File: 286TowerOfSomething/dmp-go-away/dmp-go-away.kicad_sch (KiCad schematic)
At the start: 2 parts, among them J1 Bus_ISA_16bit, U1 M6117C

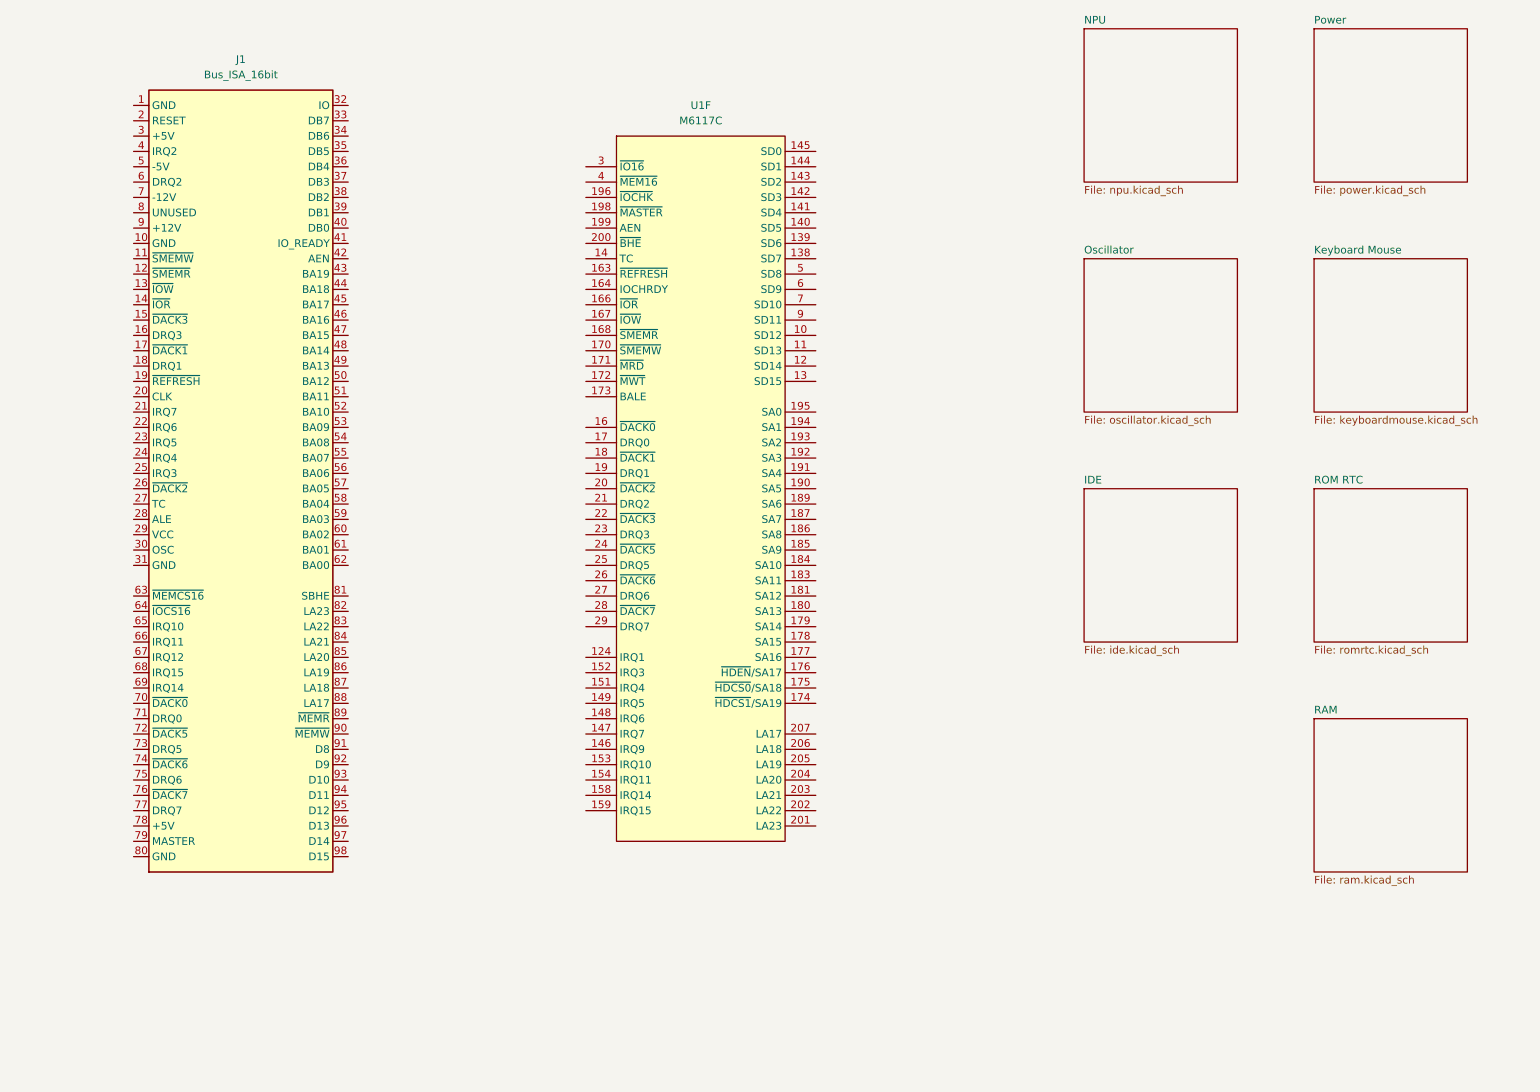
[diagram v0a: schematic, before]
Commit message: Adding work done on 386 card, coming along nicely
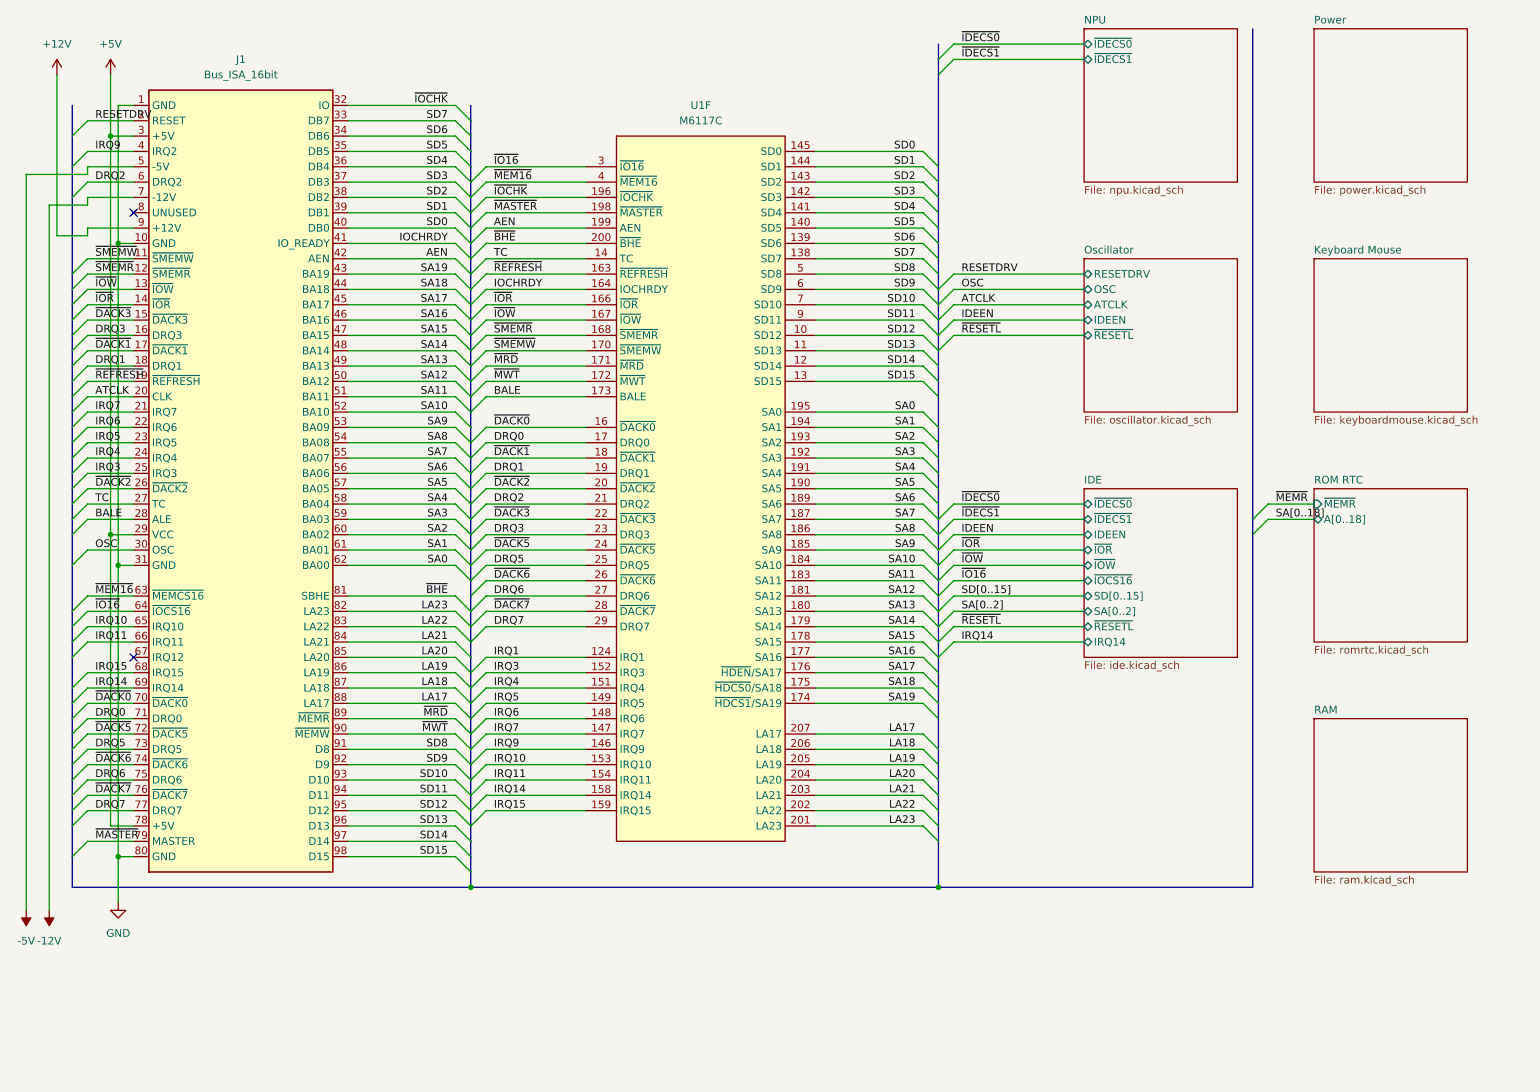
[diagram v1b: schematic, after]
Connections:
- net GND: now reaches J1.1 (GND)
- net GND: now also J1.10 (GND), J1.31 (GND), J1.80 (GND)
- net ~{SMEMW}: now reaches J1.11 (~{SMEMW})
- net ~{SMEMW}: now also U1.170 (~{SMEMW})
- net ~{SMEMR}: now reaches J1.12 (~{SMEMR})
- net ~{SMEMR}: now also U1.168 (~{SMEMR})
- net ~{IOW}: now reaches J1.13 (~{IOW})
- net ~{IOW}: now also U1.167 (~{IOW})
- net ~{IOR}: now reaches J1.14 (~{IOR})
- net ~{IOR}: now also U1.166 (~{IOR})
- net ~{DACK3}: now reaches J1.15 (~{DACK3})
- net ~{DACK3}: now also U1.22 (~{DACK3})
- net DRQ3: now reaches J1.16 (DRQ3)
- net DRQ3: now also U1.23 (DRQ3)
- net ~{DACK1}: now reaches J1.17 (~{DACK1})
- net ~{DACK1}: now also U1.18 (~{DACK1})
- net DRQ1: now reaches J1.18 (DRQ1)
- net DRQ1: now also U1.19 (DRQ1)
- net ~{REFRESH}: now reaches J1.19 (~{REFRESH})
- net ~{REFRESH}: now also U1.163 (~{REFRESH})
- net RESETDRV: now reaches J1.2 (RESET)
- net ATCLK: now reaches J1.20 (CLK)
- net IRQ7: now reaches J1.21 (IRQ7)
- net IRQ7: now also U1.147 (IRQ7)
- net IRQ6: now reaches J1.22 (IRQ6)
- net IRQ6: now also U1.148 (IRQ6)
- net IRQ5: now reaches J1.23 (IRQ5)
- net IRQ5: now also U1.149 (IRQ5)
- net IRQ4: now reaches J1.24 (IRQ4)
- net IRQ4: now also U1.151 (IRQ4)
- net IRQ3: now reaches J1.25 (IRQ3)
- net IRQ3: now also U1.152 (IRQ3)
- net ~{DACK2}: now reaches J1.26 (~{DACK2})
- net ~{DACK2}: now also U1.20 (~{DACK2})
- net TC: now reaches J1.27 (TC)
- net TC: now also U1.14 (TC)
- net BALE: now reaches J1.28 (ALE)
- net BALE: now also U1.173 (BALE)
- net +5V: now reaches J1.29 (VCC)
- net +5V: now also J1.3 (+5V), J1.78 (+5V)
- net OSC: now reaches J1.30 (OSC)
- net ~{IOCHK}: now reaches J1.32 (IO)
- net ~{IOCHK}: now also U1.196 (~{IOCHK})
- net SD7: now reaches J1.33 (DB7)
- net SD7: now also U1.138 (SD7)
- net SD6: now reaches J1.34 (DB6)
- net SD6: now also U1.139 (SD6)
- net SD5: now reaches J1.35 (DB5)
- net SD5: now also U1.140 (SD5)
- net SD4: now reaches J1.36 (DB4)
- net SD4: now also U1.141 (SD4)
- net SD3: now reaches J1.37 (DB3)
- net SD3: now also U1.142 (SD3)
- net SD2: now reaches J1.38 (DB2)
- net SD2: now also U1.143 (SD2)
- net SD1: now reaches J1.39 (DB1)
- net SD1: now also U1.144 (SD1)
- net IRQ9: now reaches J1.4 (IRQ2)
- net IRQ9: now also U1.146 (IRQ9)
- net SD0: now reaches J1.40 (DB0)
- net SD0: now also U1.145 (SD0)
- net IOCHRDY: now reaches J1.41 (IO_READY)
- net IOCHRDY: now also U1.164 (IOCHRDY)
- net AEN: now reaches J1.42 (AEN)
- net AEN: now also U1.199 (AEN)
- net SA19: now reaches J1.43 (BA19)
- net SA19: now also U1.174 (~{HDCS1}/SA19)
- net SA18: now reaches J1.44 (BA18)
- net SA18: now also U1.175 (~{HDCS0}/SA18)
- net SA17: now reaches J1.45 (BA17)
- net SA17: now also U1.176 (~{HDEN}/SA17)
- net SA16: now reaches J1.46 (BA16)
- net SA16: now also U1.177 (SA16)
- net SA15: now reaches J1.47 (BA15)
- net SA15: now also U1.178 (SA15)
- net SA14: now reaches J1.48 (BA14)
- net SA14: now also U1.179 (SA14)
- net SA13: now reaches J1.49 (BA13)
- net SA13: now also U1.180 (SA13)
- net -5V: now reaches J1.5 (-5V)
- net SA12: now reaches J1.50 (BA12)
- net SA12: now also U1.181 (SA12)
- net SA11: now reaches J1.51 (BA11)
- net SA11: now also U1.183 (SA11)
- net SA10: now reaches J1.52 (BA10)
- net SA10: now also U1.184 (SA10)
- net SA9: now reaches J1.53 (BA09)
- net SA9: now also U1.185 (SA9)
- net SA8: now reaches J1.54 (BA08)
- net SA8: now also U1.186 (SA8)
- net SA7: now reaches J1.55 (BA07)
- net SA7: now also U1.187 (SA7)
- net SA6: now reaches J1.56 (BA06)
- net SA6: now also U1.189 (SA6)
- net SA5: now reaches J1.57 (BA05)
- net SA5: now also U1.190 (SA5)
- net SA4: now reaches J1.58 (BA04)
- net SA4: now also U1.191 (SA4)
- net SA3: now reaches J1.59 (BA03)
- net SA3: now also U1.192 (SA3)
- net DRQ2: now reaches J1.6 (DRQ2)
- net DRQ2: now also U1.21 (DRQ2)
- net SA2: now reaches J1.60 (BA02)
- net SA2: now also U1.193 (SA2)
- net SA1: now reaches J1.61 (BA01)
- net SA1: now also U1.194 (SA1)
- net SA0: now reaches J1.62 (BA00)
- net SA0: now also U1.195 (SA0)
- net ~{MEM16}: now reaches J1.63 (~{MEMCS16})
- net ~{MEM16}: now also U1.4 (~{MEM16})
- net ~{IO16}: now reaches J1.64 (~{IOCS16})
- net ~{IO16}: now also U1.3 (~{IO16})
- net IRQ10: now reaches J1.65 (IRQ10)
- net IRQ10: now also U1.153 (IRQ10)
- net IRQ11: now reaches J1.66 (IRQ11)
- net IRQ11: now also U1.154 (IRQ11)
- net IRQ15: now reaches J1.68 (IRQ15)
- net IRQ15: now also U1.159 (IRQ15)
- net IRQ14: now reaches J1.69 (IRQ14)
- net IRQ14: now also U1.158 (IRQ14)
- net -12V: now reaches J1.7 (-12V)
- net ~{DACK0}: now reaches J1.70 (~{DACK0})
- net ~{DACK0}: now also U1.16 (~{DACK0})
- net DRQ0: now reaches J1.71 (DRQ0)
- net DRQ0: now also U1.17 (DRQ0)
- net ~{DACK5}: now reaches J1.72 (~{DACK5})
- net ~{DACK5}: now also U1.24 (~{DACK5})
- net DRQ5: now reaches J1.73 (DRQ5)
- net DRQ5: now also U1.25 (DRQ5)
- net ~{DACK6}: now reaches J1.74 (~{DACK6})
- net ~{DACK6}: now also U1.26 (~{DACK6})
- net DRQ6: now reaches J1.75 (DRQ6)
- net DRQ6: now also U1.27 (DRQ6)
- net ~{DACK7}: now reaches J1.76 (~{DACK7})
- net ~{DACK7}: now also U1.28 (~{DACK7})
- net DRQ7: now reaches J1.77 (DRQ7)
- net DRQ7: now also U1.29 (DRQ7)
- net ~{MASTER}: now reaches J1.79 (MASTER)
- net ~{MASTER}: now also U1.198 (~{MASTER})
- net ~{BHE}: now reaches J1.81 (SBHE)
- net ~{BHE}: now also U1.200 (~{BHE})
- net LA23: now reaches J1.82 (LA23)
- net LA23: now also U1.201 (LA23)
- net LA22: now reaches J1.83 (LA22)
- net LA22: now also U1.202 (LA22)
- net LA21: now reaches J1.84 (LA21)
- net LA21: now also U1.203 (LA21)
- net LA20: now reaches J1.85 (LA20)
- net LA20: now also U1.204 (LA20)
- net LA19: now reaches J1.86 (LA19)
- net LA19: now also U1.205 (LA19)
- net LA18: now reaches J1.87 (LA18)
- net LA18: now also U1.206 (LA18)
- net LA17: now reaches J1.88 (LA17)
- net LA17: now also U1.207 (LA17)
- net ~{MRD}: now reaches J1.89 (~{MEMR})
- net ~{MRD}: now also U1.171 (~{MRD})
- net +12V: now reaches J1.9 (+12V)
- net ~{MWT}: now reaches J1.90 (~{MEMW})
- net ~{MWT}: now also U1.172 (~{MWT})
- net SD8: now reaches J1.91 (D8)
- net SD8: now also U1.5 (SD8)
- net SD9: now reaches J1.92 (D9)
- net SD9: now also U1.6 (SD9)
- net SD10: now reaches J1.93 (D10)
- net SD10: now also U1.7 (SD10)
- net SD11: now reaches J1.94 (D11)
- net SD11: now also U1.9 (SD11)
- net SD12: now reaches J1.95 (D12)
- net SD12: now also U1.10 (SD12)
- net SD13: now reaches J1.96 (D13)
- net SD13: now also U1.11 (SD13)
- net SD14: now reaches J1.97 (D14)
- net SD14: now also U1.12 (SD14)
- net SD15: now reaches J1.98 (D15)
- net SD15: now also U1.13 (SD15)
- net IRQ1: now reaches U1.124 (IRQ1)
- no-connect marks 0 -> 2
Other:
- sheet IDE ports: added IDEEN, IRQ14, SA[0..2], SD[0..15], ~{IDECS0}, ~{IDECS1}, ~{IOCS16}, ~{IOR}, ~{IOW}, ~{RESETL}; removed none
- sheet NPU ports: added ~{IDECS0}, ~{IDECS1}; removed none
- sheet Oscillator ports: added ATCLK, IDEEN, OSC, RESETDRV, ~{RESETL}; removed none
- sheet ROM RTC ports: added A[0..18], ~{MEMR}; removed none

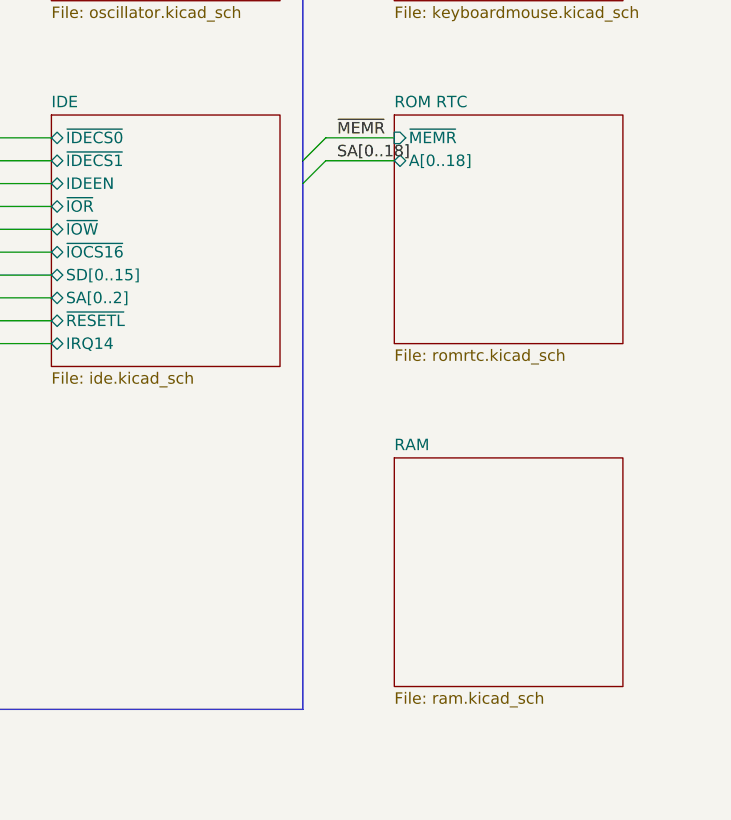
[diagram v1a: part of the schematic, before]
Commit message: Adding some missing caps, and the optional DS12885 RTC for dmp-go-away
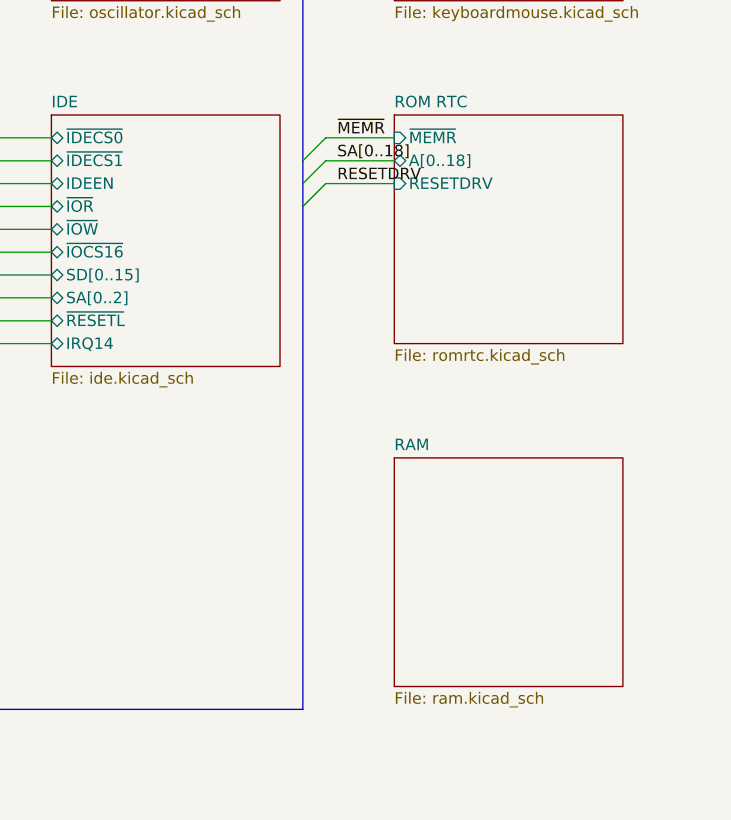
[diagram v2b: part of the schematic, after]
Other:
- sheet ROM RTC ports: added RESETDRV; removed none
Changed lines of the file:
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@@
 	)
 	(bus_entry
+		(at 220.98 109.22)
+		(size -2.54 2.54)
+		(stroke
+			(width 0)
+			(type default)
+		)
+	)
+	(bus_entry
 		(at 25.4 63.5)
 		(size -2.54 2.54)
@@
 	(wire
 		(pts
+			(xy 220.98 109.22) (xy 228.6 109.22)
+		)
+		(stroke
+			(width 0)
+			(type default)
+		)
+	)
+	(wire
+		(pts
 			(xy 68.58 60.96) (xy 86.36 60.96)
 		)
@@
 	(bus
 		(pts
+			(xy 218.44 111.76) (xy 218.44 167.64)
+		)
+		(stroke
+			(width 0)
+			(type default)
+		)
+	)
+	(bus
+		(pts
 			(xy 88.9 114.3) (xy 88.9 116.84)
 		)
@@
 	(bus
 		(pts
-			(xy 218.44 109.22) (xy 218.44 167.64)
+			(xy 218.44 109.22) (xy 218.44 111.76)
 		)
 		(stroke
@@
 		)
 	)
+	(label "RESETDRV"
+		(at 222.25 109.22 0)
+		(fields_autoplaced yes)
+		(effects
+			(font
+				(size 1.27 1.27)
+			)
+			(justify left bottom)
+		)
+	)
 	(label "~{MWT}"
 		(at 85.09 142.24 180)
@@
 			(effects
 				(font
+					(size 1.27 1.27)
+				)
+				(justify left)
+			)
+		)
+		(pin "RESETDRV" input
+			(at 228.6 109.22 180)
+			(effects
+				(font

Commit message: Added footprints and started figuring out layout for dmp-go-away
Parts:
- J1: footprint (none) -> Connector_PCBEdge:BUS_AT
- U1: footprint (none) -> Package_QFP:PQFP-208_28x28mm_P0.5mm
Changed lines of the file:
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@@
 			)
 		)
-		(property "Footprint" ""
+		(property "Footprint" "Connector_PCBEdge:BUS_AT"
 			(at 50.8 100.33 0)
 			(effects
@@
 			)
 		)
-		(property "Footprint" ""
+		(property "Footprint" "Package_QFP:PQFP-208_28x28mm_P0.5mm"
 			(at 127 101.6 0)
 			(effects

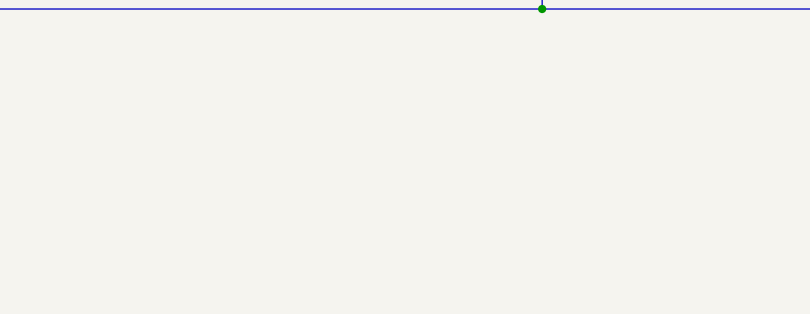
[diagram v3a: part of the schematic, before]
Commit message: Adding bracket to dmp-go-away
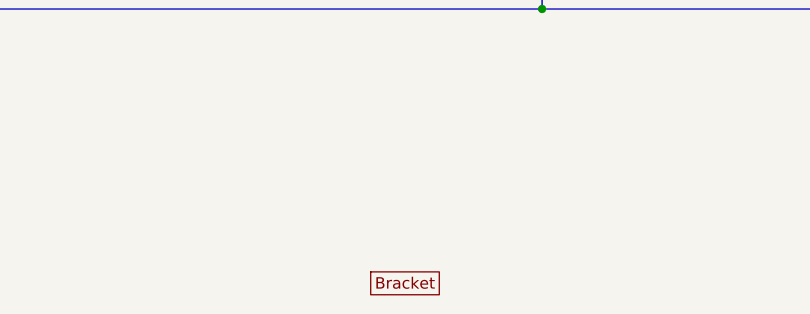
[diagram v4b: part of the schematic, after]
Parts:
- added BRACKET1: ~, pc-parts:PC_BRACKET_ISA_KEYSTONE_9202_Rev1, symbol pc-parts:9202
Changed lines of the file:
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@@
+	)
+	(symbol
+		(lib_id "pc-parts:9202")
+		(at 151.13 198.12 0)
+		(unit 1)
+		(exclude_from_sim no)
+		(in_bom yes)
+		(on_board yes)
+		(dnp no)
+		(fields_autoplaced yes)
+		(property "Reference" "BRACKET1"
+			(at 151.13 198.12 0)
+			(effects
+				(font
+					(size 1.27 1.27)
+				)
+				(hide yes)
+			)
+		)
+		(property "Value" "~"
+			(at 156.21 198.12 0)
+			(effects
+				(font
+					(size 1.27 1.27)
+				)
+				(justify left)
+			)
+		)
+		(property "Footprint" "pc-parts:PC_BRACKET_ISA_KEYSTONE_9202_Rev1"
+			(at 151.13 198.12 0)
+			(effects
+				(font
+					(size 1.27 1.27)
+				)
+				(hide yes)
+			)
+		)
+		(property "Datasheet" ""
+			(at 151.13 198.12 0)
+			(effects
+				(font
+					(size 1.27 1.27)
+				)
+				(hide yes)
+			)
+		)
+		(property "Description" ""
+			(at 151.13 198.12 0)
+			(effects
+				(font
+					(size 1.27 1.27)
+				)
+				(hide yes)
+			)
+		)
+		(instances
+			(project ""
+				(path "/b66cfc40-8652-41e7-bd5f-f23cb0cb78db"
+					(reference "BRACKET1")
+					(unit 1)
+				)
+			)
+		)
 	)
 	(symbol
